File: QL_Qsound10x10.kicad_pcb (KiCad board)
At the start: 2 copper layers, 99.1 x 99.1 mm, 23 parts, among them J1 QL_SLOT_DIN41612_CARD, J2 Conn_02x17_Odd_Even, J3 AudioJack2_Ground_Switch, J4 Conn_01x01_Female, Q1 PN2222A, U1 L7805, U2 74LS10, U3 74LS266, U4 2764, U5 74LS03, U6 PSG_AY-3-8910, U7 6821

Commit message: complete strings in pcb
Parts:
- R1: value 100k -> 2k2
- U4: value 2764 -> W27C512
- U6: value PSG_AY-3-8910 -> AY-3-8910
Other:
- board text added: "Iöts"
- board text added: "RE-QSP"
- board text added: "T"
- board text added: "© MCMLXXXVI J.Merz + J.Reintsch"
- board text removed: "(C) MCMLXXXVI J. J.Reintsch"

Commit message: Update, now work all
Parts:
- Q1: value PN2222A -> 2N2222A
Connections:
- J1 pad b25: unconnected-(J1-Padb25) -> /DTACK
- U5 pad 11: unconnected-(U5-Pad11) -> Net-(U5-Pad4)
- U5 pad 12: unconnected-(U5-Pad12) -> /E
- U5 pad 13: unconnected-(U5-Pad13) -> /E
- U5 pad 2: /E -> /DS
- U5 pad 4: Net-(Q1-Pad2) -> Net-(U5-Pad4)
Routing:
- net /E: track 162.8 -> 176.9 mm
- net /CS2/OE: track 240.4 -> 231.7 mm, vias 2 -> 3
- net Net-(U5-Pad4): track 0.00 -> 7.62 mm
- net Net-(Q1-Pad2): track 64.3 -> 59.3 mm
- net /DS: track 98.1 -> 100.6 mm

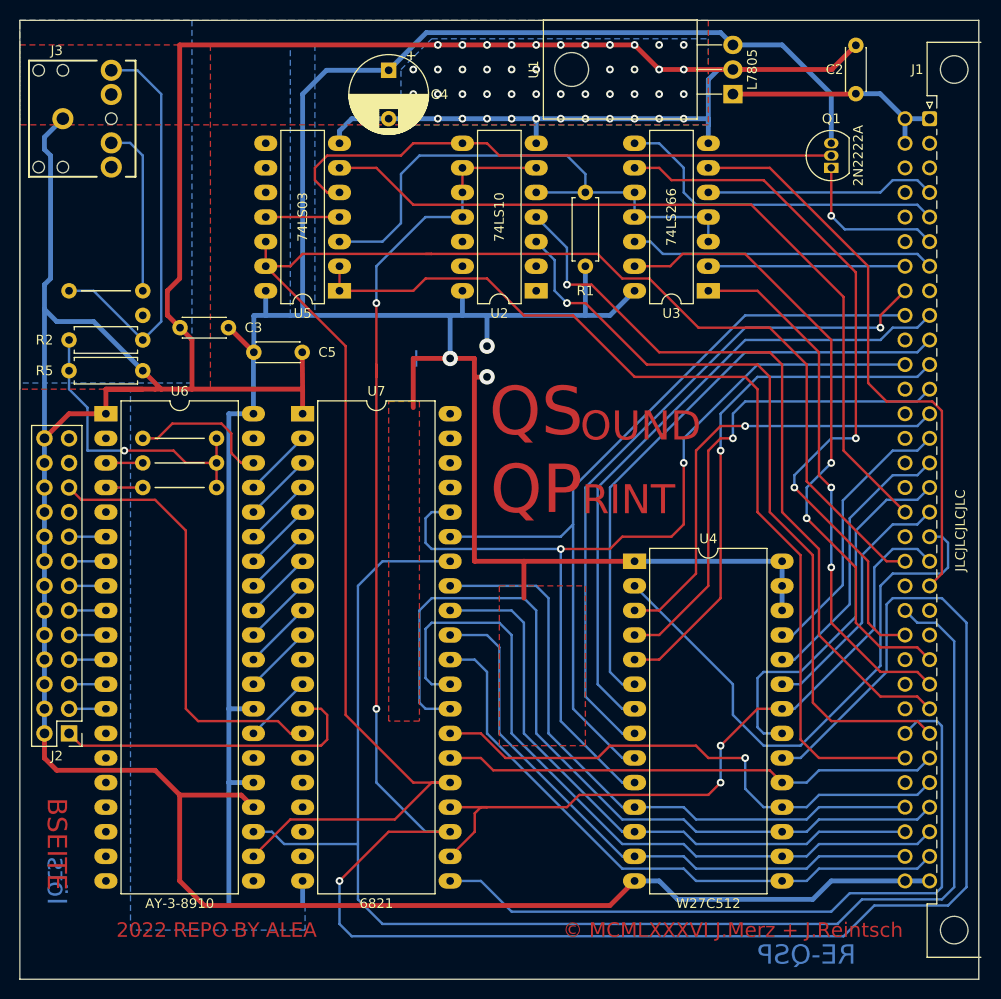
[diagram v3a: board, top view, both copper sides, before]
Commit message: tracks more similar to original
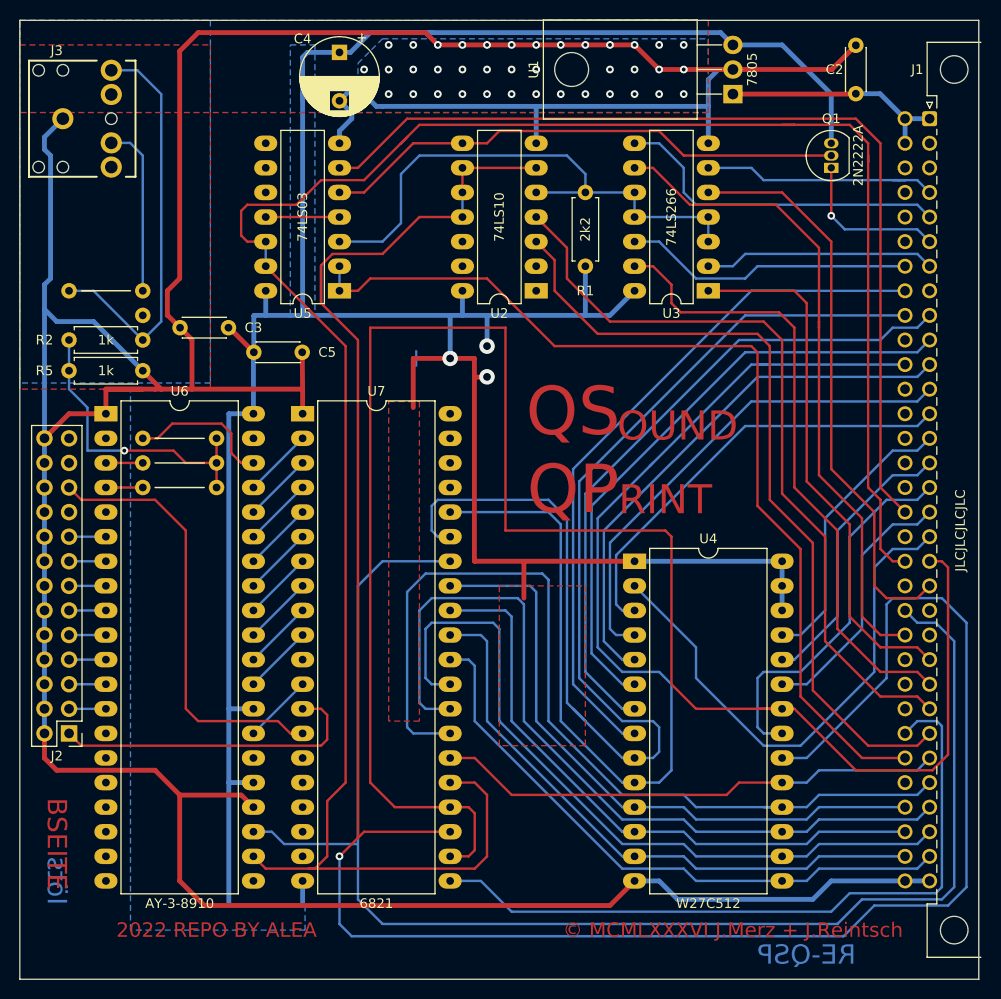
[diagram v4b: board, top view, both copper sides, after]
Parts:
- U1: value L7805 -> 7805
- moved C4 5.41 mm to (129.5, 46.5)
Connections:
- U3 pad 1: /A17 -> /A16
- U3 pad 12: /SP2 -> /SP3
- U3 pad 13: /A16 -> /A17
- U3 pad 2: /SP3 -> /SP2
- U3 pad 5: /SP0 -> /A14
- U3 pad 6: /A14 -> /SP0
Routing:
- net /A13: track 74.1 -> 190.3 mm, vias 2 -> 0
- net /E: track 176.9 -> 228.9 mm
- net /A1: track 86.2 -> 126.7 mm
- net /D6: track 56.7 -> 94.9 mm, vias 1 -> 0
- net /A0: track 96.3 -> 118.3 mm, vias 2 -> 0
- net /VPA: track 82.4 -> 98.2 mm
- net /A16: track 66.1 -> 55.0 mm, vias 2 -> 0
- net /A17: track 55.3 -> 65.1 mm, vias 2 -> 0
- net /SP3: track 20.3 -> 30.0 mm
- net /CS2/OE: track 231.7 -> 239.5 mm, vias 3 -> 1
- net /SP2: track 31.5 -> 23.9 mm
- net GND: track 398.7 -> 405.7 mm, vias 45 -> 39
- net /A15: track 75.1 -> 68.3 mm, vias 2 -> 0
- net Net-(Q1-Pad2): track 59.3 -> 54.5 mm
- net /A12: track 58.3 -> 54.4 mm
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
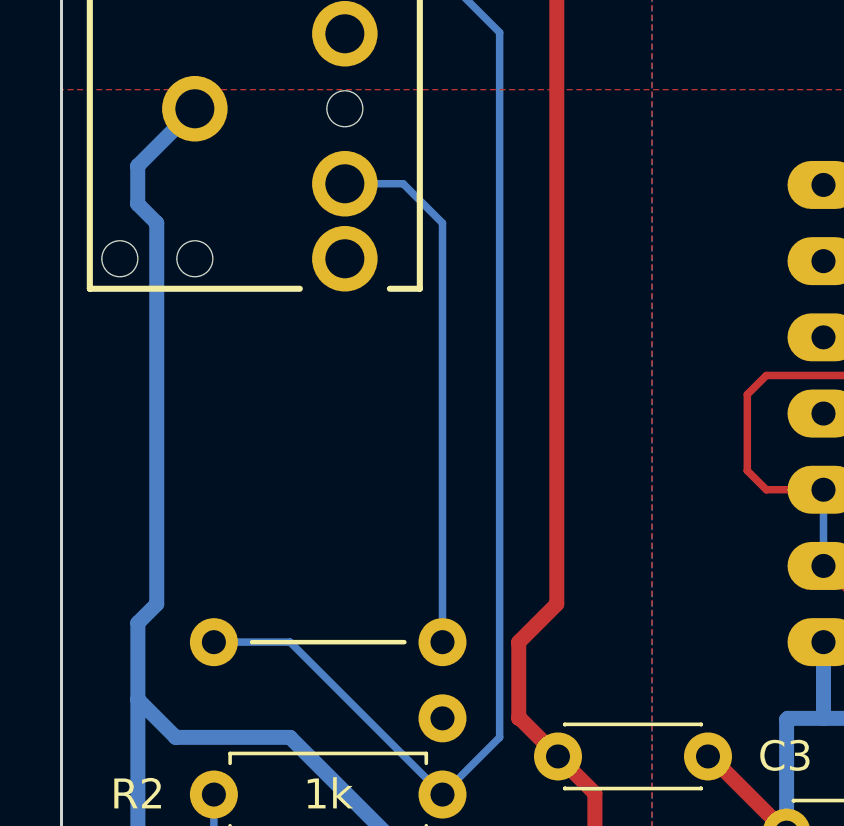
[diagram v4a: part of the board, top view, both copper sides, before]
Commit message: Update some errors in PCB
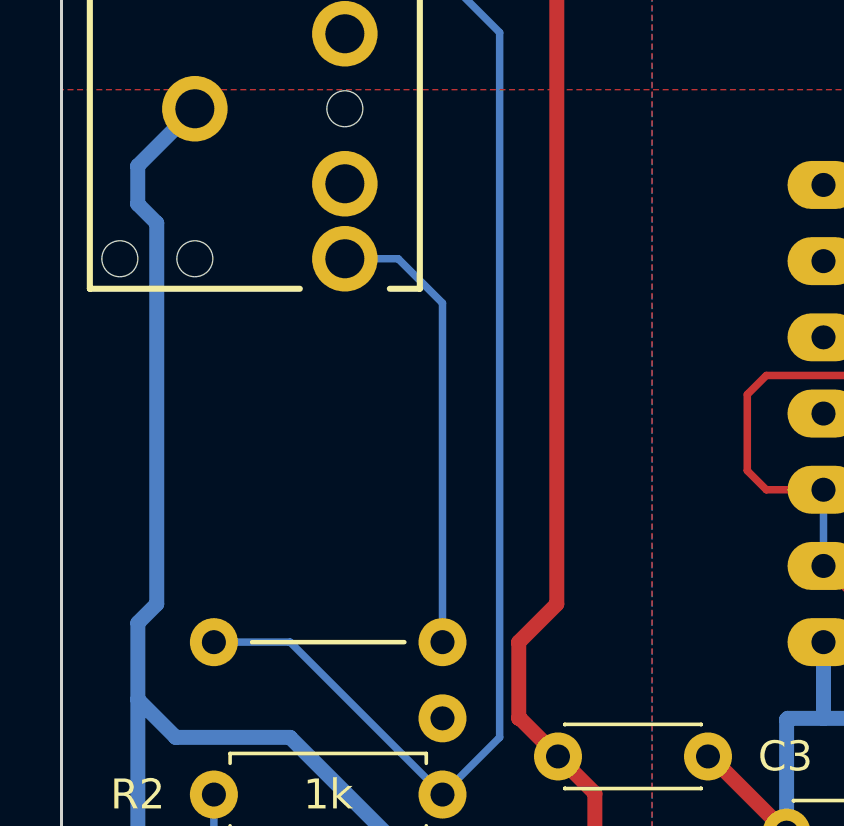
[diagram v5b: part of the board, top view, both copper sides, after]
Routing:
- net Net-(J3-PadT): track 17.8 -> 15.2 mm

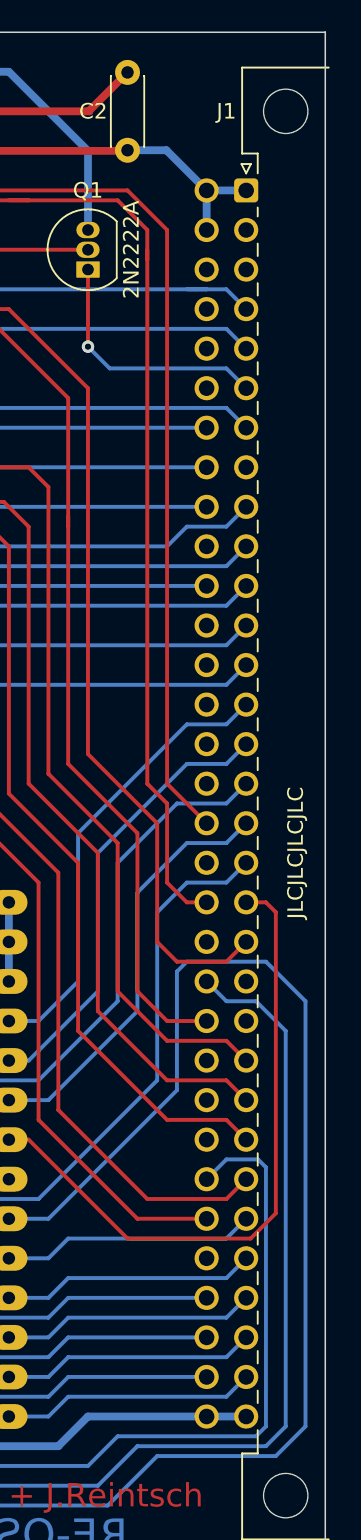
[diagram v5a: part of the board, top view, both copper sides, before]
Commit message: Updated pins on QL conector
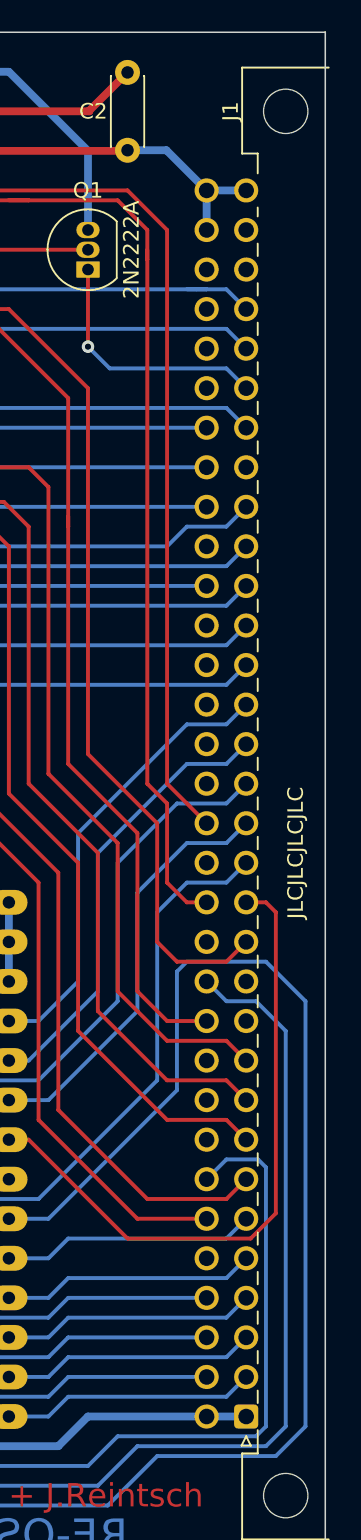
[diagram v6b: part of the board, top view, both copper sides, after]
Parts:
- J1: footprint 8bits:DIN41612_B_2x32_Male_Horizontal_THT -> 8bits:DIN41612_B_2x32_Female_Horizontal_THT
- moved J1 78.7 mm to (190.5, 132.1)
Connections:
- J1 pad a1: +9V -> GND
- J1 pad a10: /A4 -> /A16
- J1 pad a11: /A5 -> unconnected-(J1-CLKCPU-Pada11)
- J1 pad a12: /A6 -> unconnected-(J1-RED-Pada12)
- J1 pad a13: /A7 -> /A14
- J1 pad a14: /A8 -> /A13
- J1 pad a15: /A9 -> /A12
- J1 pad a16: /A10 -> /A11
- J1 pad a17: /A11 -> /A10
- J1 pad a18: /A12 -> /A9
- J1 pad a19: /A13 -> /A8
- J1 pad a2: unconnected-(J1-Pada2) -> /D3
- J1 pad a20: /A14 -> /A7
- J1 pad a21: unconnected-(J1-Pada21) -> /A6
- J1 pad a22: unconnected-(J1-Pada22) -> /A5
- J1 pad a23: /A16 -> /A4
- J1 pad a24: /A17 -> /A3
- J1 pad a25: /A18 -> unconnected-(J1-~{DBG}-Pada25)
- J1 pad a26: /A19 -> /SP2
- J1 pad a27: /D7 -> /DSMC
- J1 pad a28: /D6 -> /SP1
- J1 pad a29: /D5 -> /SP0
- J1 pad a3: unconnected-(J1-Pada3) -> /D4
- J1 pad a30: /D4 -> unconnected-(J1-+12V-Pada30)
- J1 pad a31: /D3 -> unconnected-(J1--12V-Pada31)
- J1 pad a32: GND -> +9V
- J1 pad a4: /SP0 -> /D5
- J1 pad a5: /SP1 -> /D6
- J1 pad a6: /DSMC -> /D7
- J1 pad a7: /SP2 -> /A19
- J1 pad a8: unconnected-(J1-Pada8) -> /A18
- J1 pad a9: /A3 -> /A17
- J1 pad b1: +9V -> GND
- J1 pad b11: /A0 -> /A15
- J1 pad b12: unconnected-(J1-Padb12) -> /RESET
- J1 pad b14: unconnected-(J1-Padb14) -> /E
- J1 pad b16: unconnected-(J1-Padb16) -> /VPA
- J1 pad b17: /VPA -> unconnected-(J1-GREEN-Padb17)
- J1 pad b19: /E -> unconnected-(J1-FC2-Padb19)
- J1 pad b2: +9V -> /D2
- J1 pad b21: /RESET -> unconnected-(J1-FC0-Padb21)
- J1 pad b22: /A15 -> /A0
- J1 pad b24: unconnected-(J1-Padb24) -> /A1
- J1 pad b25: /DTACK -> /A2
- J1 pad b26: /RW -> /SP3
- J1 pad b27: /DS -> unconnected-(J1-~{IPLO}-Padb27)
- J1 pad b29: /D0 -> unconnected-(J1-~{IPL1}-Padb29)
- J1 pad b3: unconnected-(J1-Padb3) -> /D1
- J1 pad b30: /D1 -> unconnected-(J1-~{EXTINT}-Padb30)
- J1 pad b31: /D2 -> +9V
- J1 pad b32: GND -> +9V
- J1 pad b4: unconnected-(J1-Padb4) -> /D0
- J1 pad b6: unconnected-(J1-Padb6) -> /DS
- J1 pad b7: /SP3 -> /RW
- J1 pad b8: /A2 -> unconnected-(J1-~{DTACK}-Padb8)
- J1 pad b9: /A1 -> unconnected-(J1-~{BG}-Padb9)

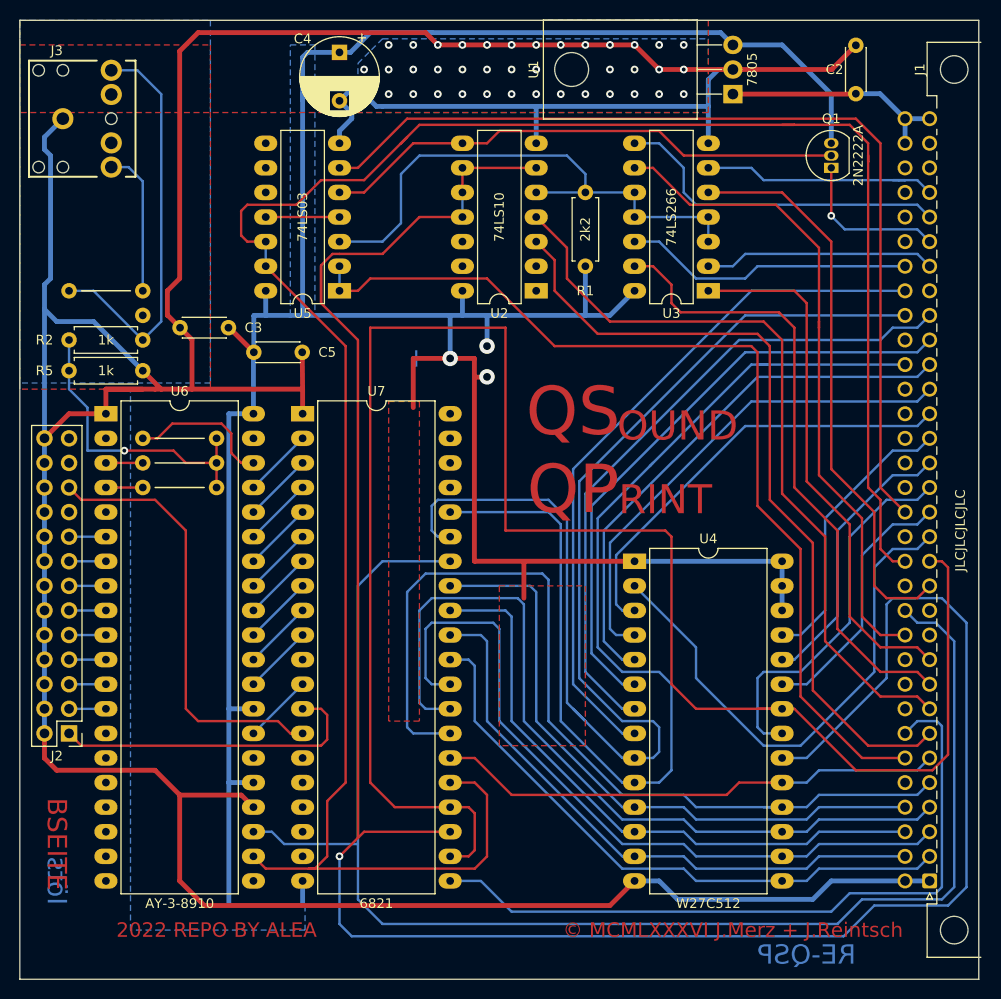
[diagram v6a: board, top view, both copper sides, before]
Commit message: move 7805 down
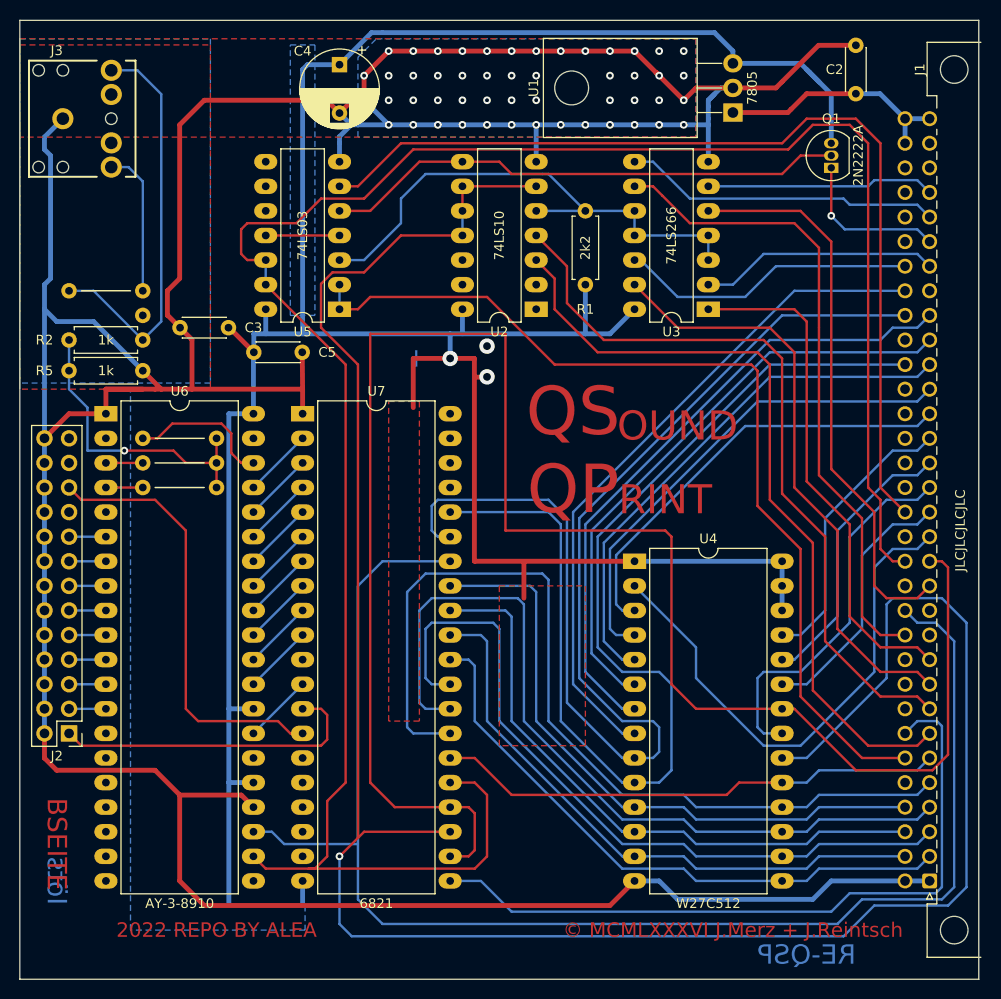
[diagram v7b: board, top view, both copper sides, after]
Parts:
- moved R1 1.91 mm to (154.9, 70.5)
- moved U1 1.91 mm to (170.2, 52.7)
- moved U2 1.91 mm to (149.9, 73.0)
- moved U3 1.91 mm to (167.6, 73.0)
- moved U5 1.91 mm to (129.5, 73.0)
- moved C4 1.27 mm to (129.5, 47.8)
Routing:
- net /CS2/OE: track 239.5 -> 233.8 mm
- net /A1: track 126.7 -> 122.7 mm
- net /E: track 228.9 -> 225.0 mm
- net VCC: track 306.0 -> 302.2 mm
- net /A13: track 190.3 -> 186.4 mm
- net /A17: track 65.1 -> 61.7 mm
- net /A0: track 118.3 -> 115.5 mm
- net Net-(R1-Pad2): track 57.6 -> 55.0 mm
- net /A2: track 72.6 -> 70.0 mm
- net /SP1: track 35.1 -> 32.8 mm
- net /DS: track 100.2 -> 98.3 mm
- net /D6: track 94.9 -> 93.0 mm
- net /A16: track 55.0 -> 53.1 mm
- net /A19: track 82.8 -> 80.9 mm
- net /A3: track 68.3 -> 66.4 mm
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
